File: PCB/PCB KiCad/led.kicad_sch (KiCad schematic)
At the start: 20 parts, among them J3 Conn_01x04, J4 Conn_01x04, U3 TLC59208FIPWR

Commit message: Minor schematic cleanup!
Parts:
- added R14: 1k, Resistor_SMD:R_0805_2012Metric_Pad1.20x1.40mm_HandSolder, symbol Device:R
- renumbered C14 to C16, D9 to D10, D10 to D11, D3 to D4, D4 to D5, D5 to D6, D6 to D7, D7 to D8, D8 to D9, J3 to J4, J4 to J5, R8 to R15, R9 to R16, R10 to R17, R11 to R18, R12 to R19, R13 to R20, R14 to R21, R15 to R22, U3 to U4
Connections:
- net LED_RESET: now reaches U4.13 (~{RESET})
- net LED_RESET: now also R14.1
- net +3V3 renamed +3.3V
- net +3.3V: now also R14.2
- no-connect marks 1 -> 0
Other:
- moved on the sheet: C16, D10, D11, D4, D5, D6, D7, D8, D9, J4, J5, R15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

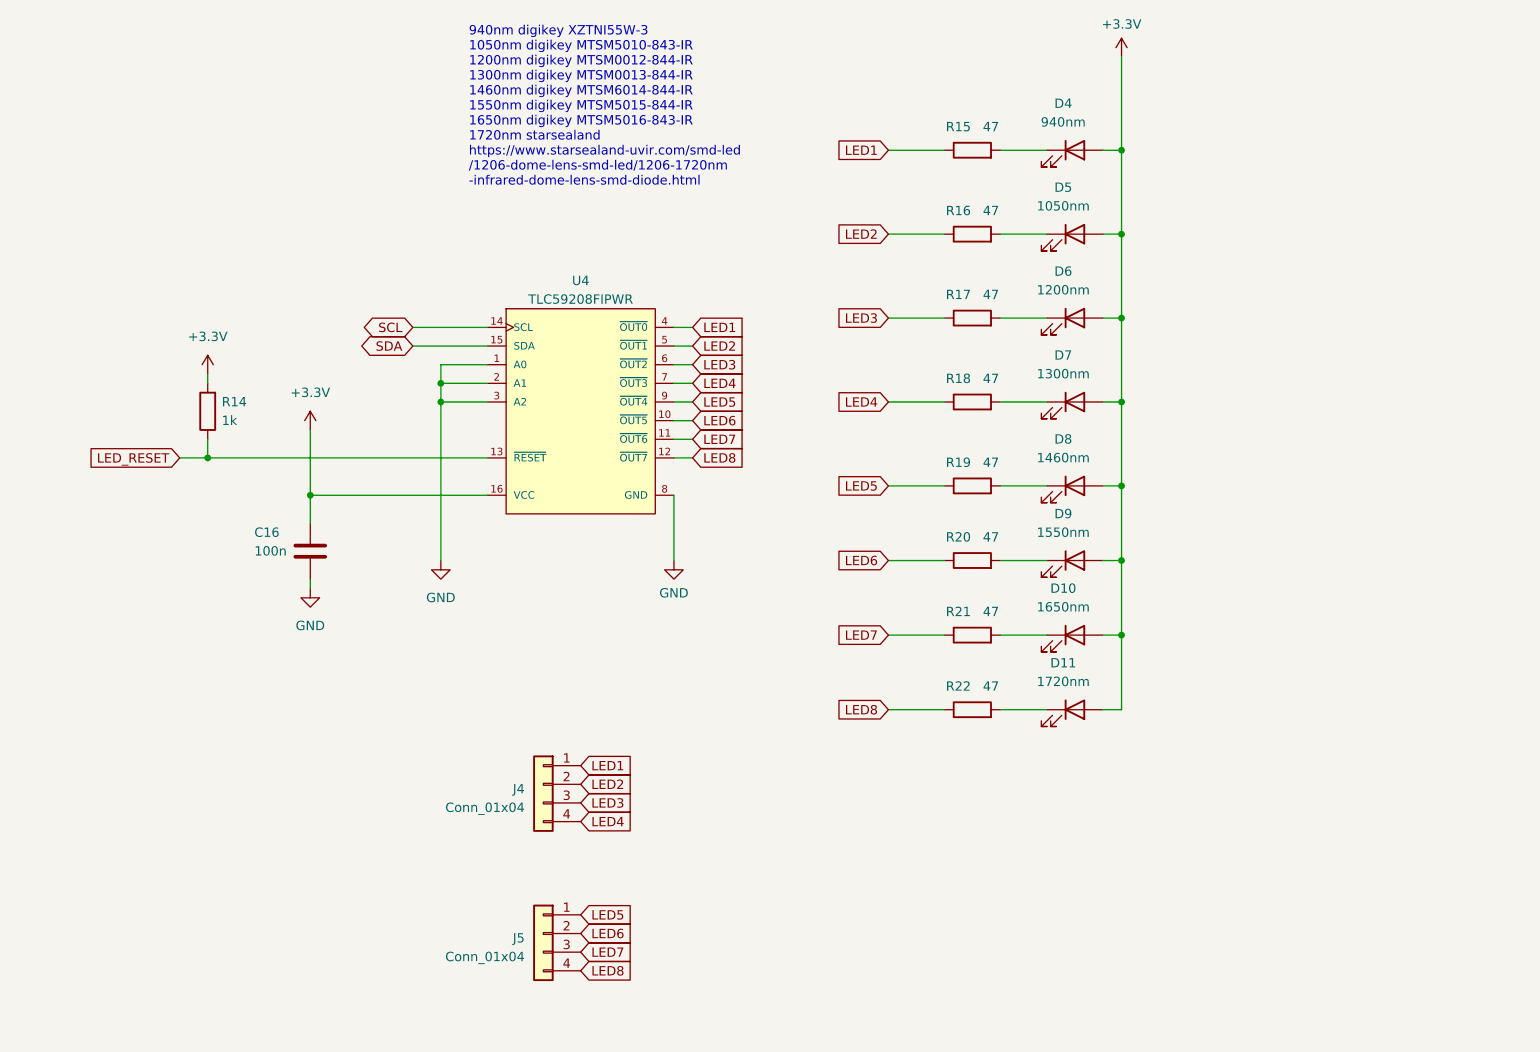
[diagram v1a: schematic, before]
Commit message: Giant schematic cleanup to make more sense of the sensor circuit and just clean everything up a bit.
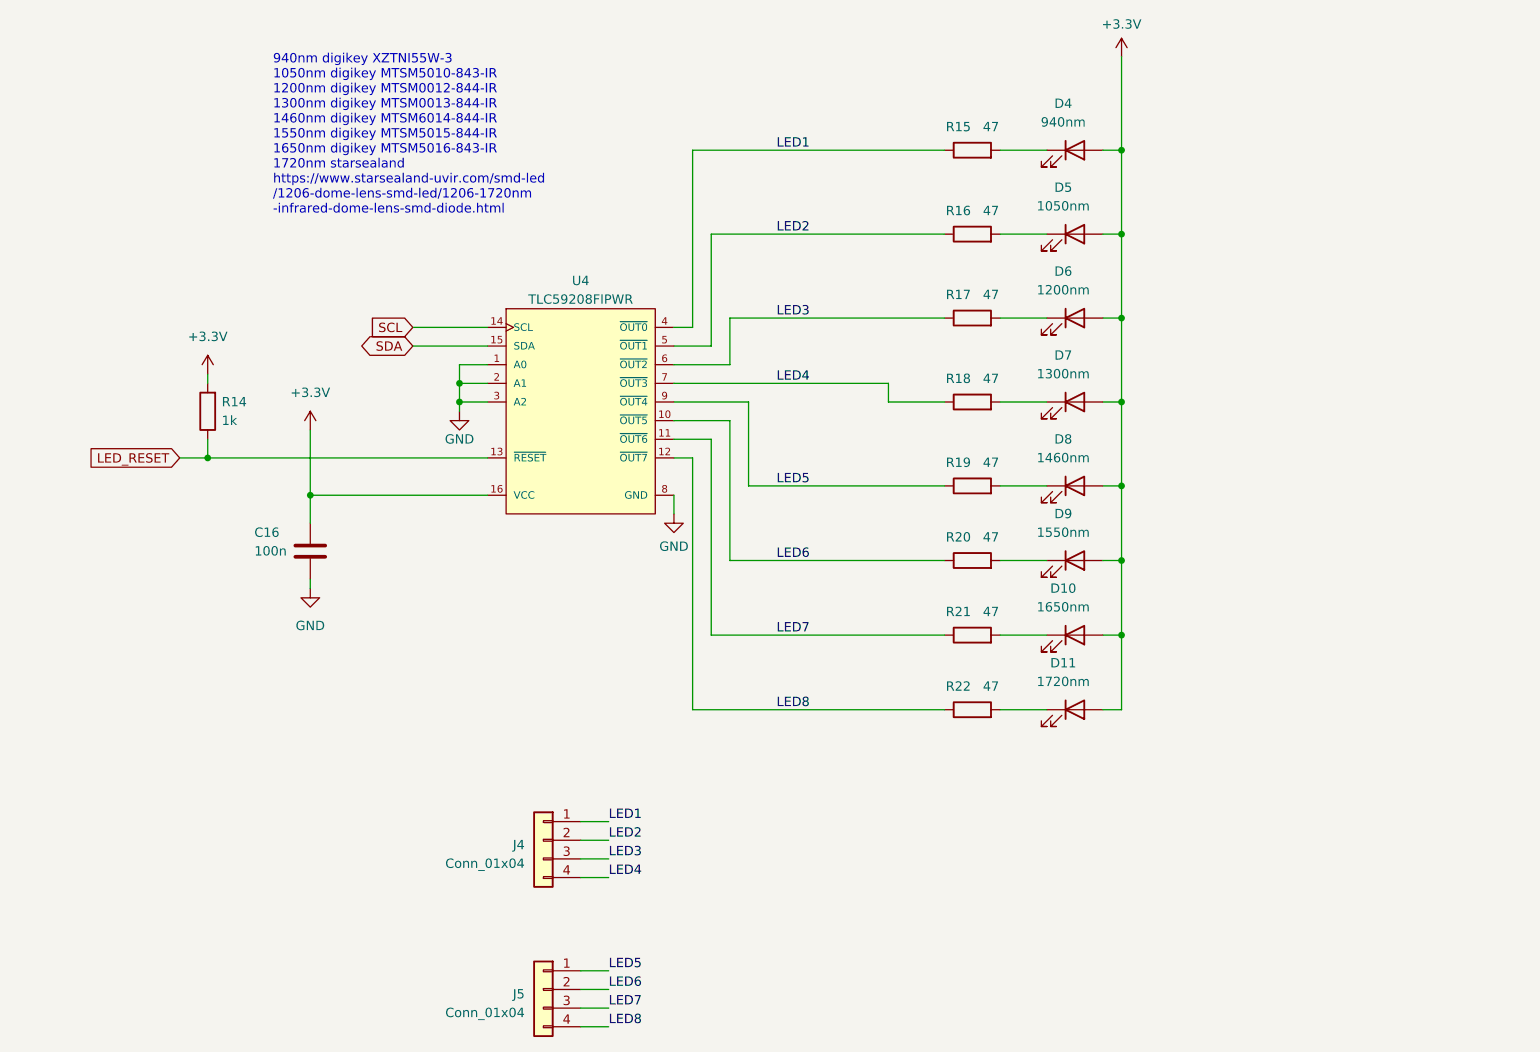
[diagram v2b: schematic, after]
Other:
- moved on the sheet: J4, J5

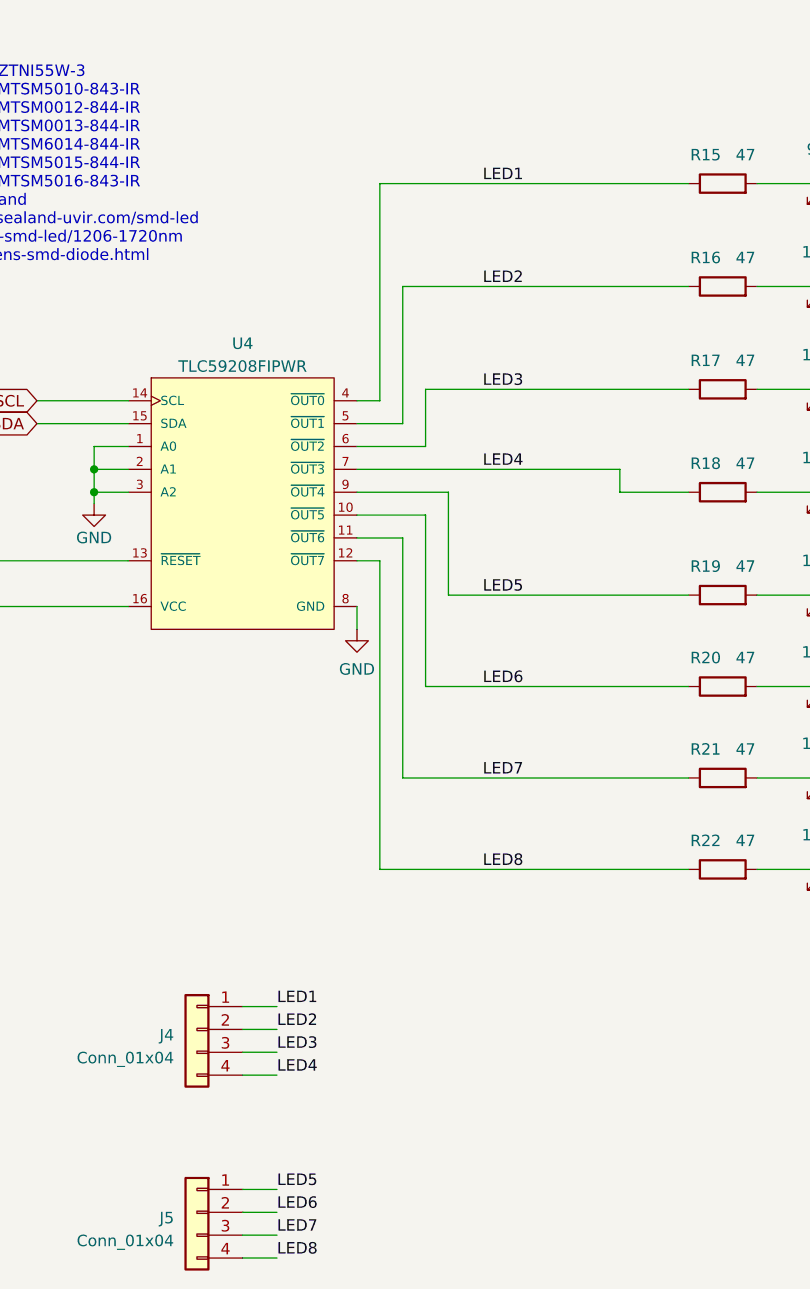
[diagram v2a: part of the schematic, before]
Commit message: Relabel LEDs 0 - 7 and put that on the silkscreen for reference.
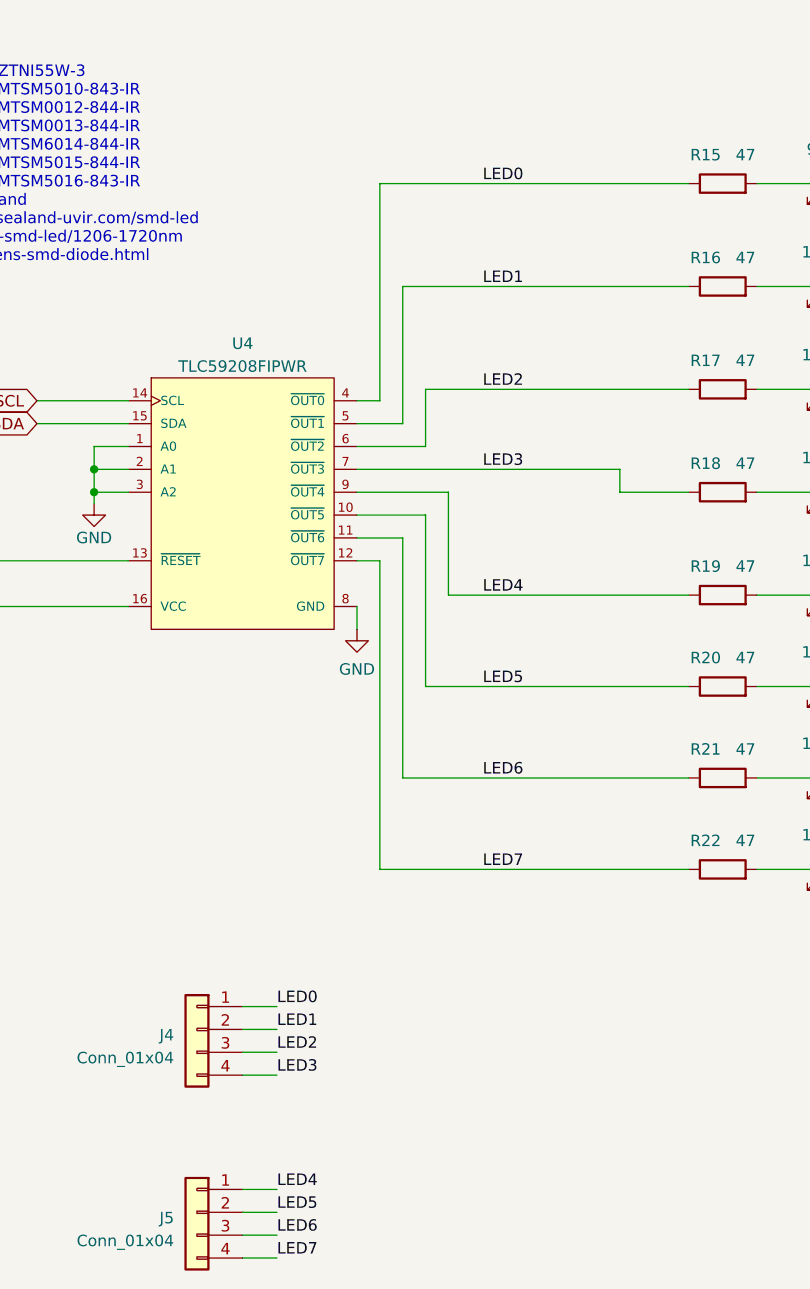
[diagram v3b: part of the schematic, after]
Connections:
- net LED8 is gone; now on net LED7: J5.4 (Pin_4), R22.1, U4.12 (~{OUT7})
- net LED1: now also J4.2 (Pin_2), R16.1, U4.5 (~{OUT1}); no longer J4.1 (Pin_1), R15.1, U4.4 (~{OUT0})
- net LED2: now also J4.3 (Pin_3), R17.1, U4.6 (~{OUT2}); no longer J4.2 (Pin_2), R16.1, U4.5 (~{OUT1})
- net LED3: now also J4.4 (Pin_4), R18.1, U4.7 (~{OUT3}); no longer J4.3 (Pin_3), R17.1, U4.6 (~{OUT2})
- net LED4: now also J5.1 (Pin_1), R19.1, U4.9 (~{OUT4}); no longer J4.4 (Pin_4), R18.1, U4.7 (~{OUT3})
- net LED5: now also J5.2 (Pin_2), R20.1, U4.10 (~{OUT5}); no longer J5.1 (Pin_1), R19.1, U4.9 (~{OUT4})
- net LED6: now also J5.3 (Pin_3), R21.1, U4.11 (~{OUT6}); no longer J5.2 (Pin_2), R20.1, U4.10 (~{OUT5})
- net LED7: no longer J5.3 (Pin_3), R21.1, U4.11 (~{OUT6})
- new net LED0: J4.1 (Pin_1), R15.1, U4.4 (~{OUT0})
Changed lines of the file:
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@@
 		)
 	)
-	(label "LED3"
+	(label "LED2"
 		(at 137.16 146.05 0)
 		(effects
@@
 		)
 	)
-	(label "LED4"
+	(label "LED3"
 		(at 137.16 148.59 0)
 		(effects
@@
 		)
 	)
-	(label "LED3"
+	(label "LED2"
 		(at 160.02 72.39 0)
 		(effects
@@
 		)
 	)
-	(label "LED2"
+	(label "LED1"
 		(at 137.16 143.51 0)
 		(effects
@@
 		)
 	)
-	(label "LED1"
+	(label "LED0"
 		(at 160.02 49.53 0)
 		(effects
@@
 		)
 	)
-	(label "LED7"
+	(label "LED6"
 		(at 160.02 115.57 0)
 		(effects
@@
 		)
 	)
-	(label "LED7"
+	(label "LED6"
 		(at 137.16 166.37 0)
 		(effects
@@
 		)
 	)
-	(label "LED8"
+	(label "LED7"
 		(at 160.02 125.73 0)
 		(effects
@@
 		)
 	)
-	(label "LED5"
+	(label "LED4"
 		(at 160.02 95.25 0)
 		(effects
@@
 		)
 	)
-	(label "LED1"
+	(label "LED0"
 		(at 137.16 140.97 0)
 		(effects
@@
 		)
 	)
-	(label "LED6"
+	(label "LED5"
 		(at 137.16 163.83 0)
 		(effects
@@
 		)
 	)
-	(label "LED8"
+	(label "LED7"
 		(at 137.16 168.91 0)
 		(effects
@@
 		)
 	)
-	(label "LED2"
+	(label "LED1"
 		(at 160.02 60.96 0)
 		(effects
@@
 		)
 	)
-	(label "LED4"
+	(label "LED3"
 		(at 160.02 81.28 0)
 		(effects
@@
 		)
 	)
-	(label "LED5"
+	(label "LED4"
 		(at 137.16 161.29 0)
 		(effects
@@
 		)
 	)
-	(label "LED6"
+	(label "LED5"
 		(at 160.02 105.41 0)
 		(effects
